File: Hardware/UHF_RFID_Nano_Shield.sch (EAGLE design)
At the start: 35 parts, among them J2 FTDI, J3 JST, J4 U.FL, J5 Extra, J6 Screw Terminal, J7 GPIOs, U1 Nano, U2 TXB0104, U3 TVS_DIODE_ARRAY

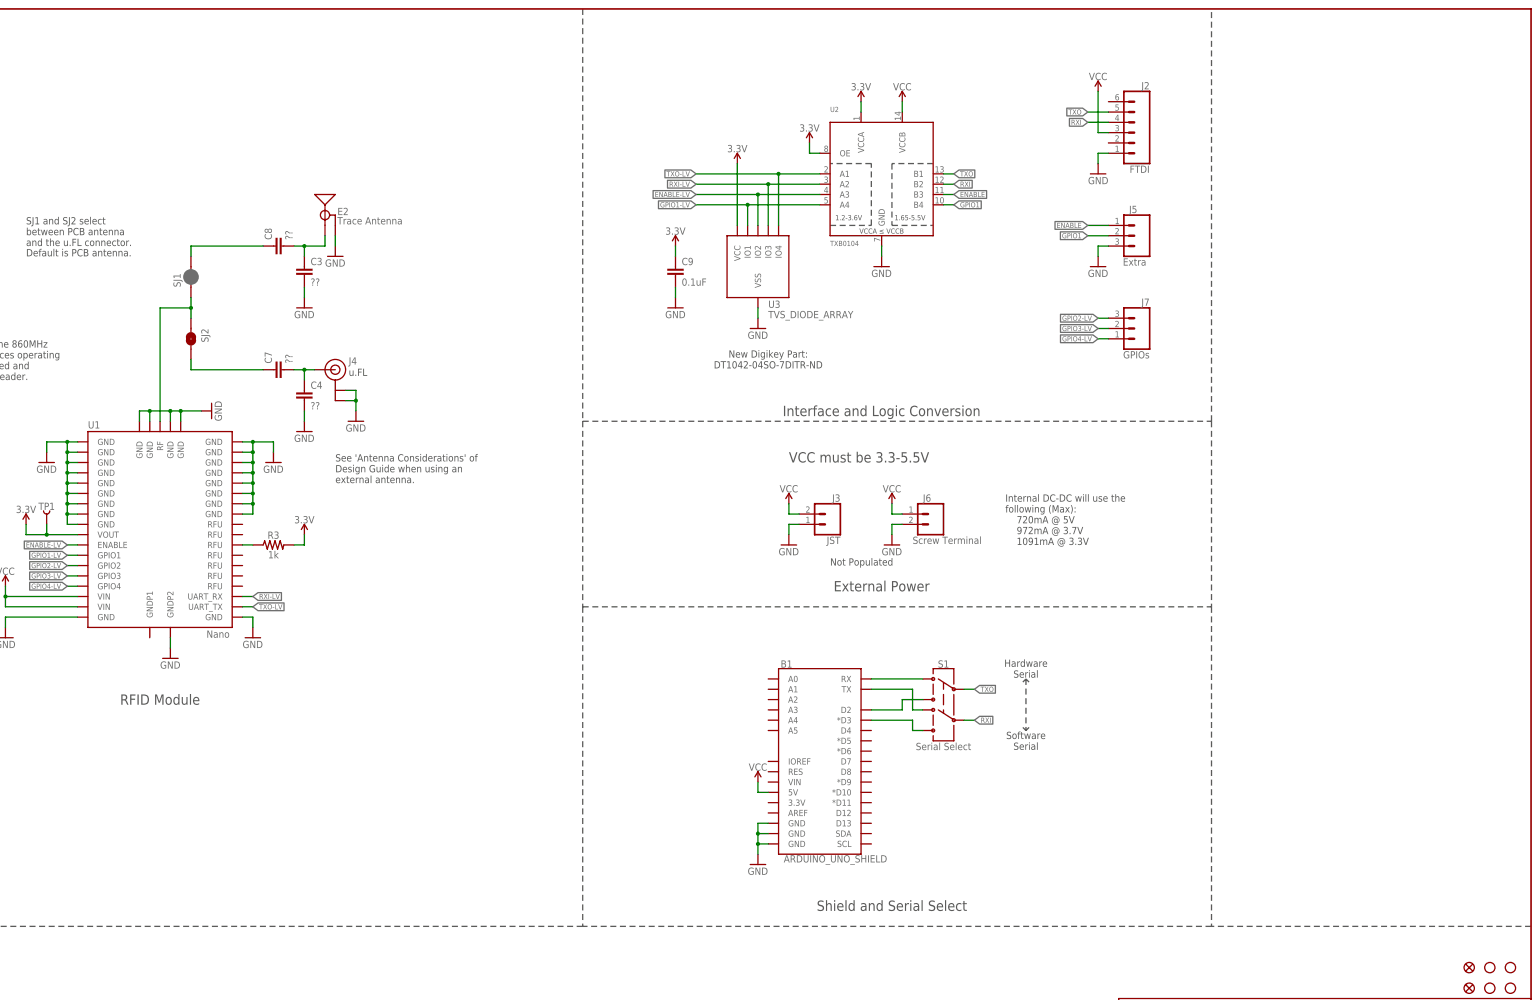
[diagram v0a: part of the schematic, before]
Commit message: Many changes from design review
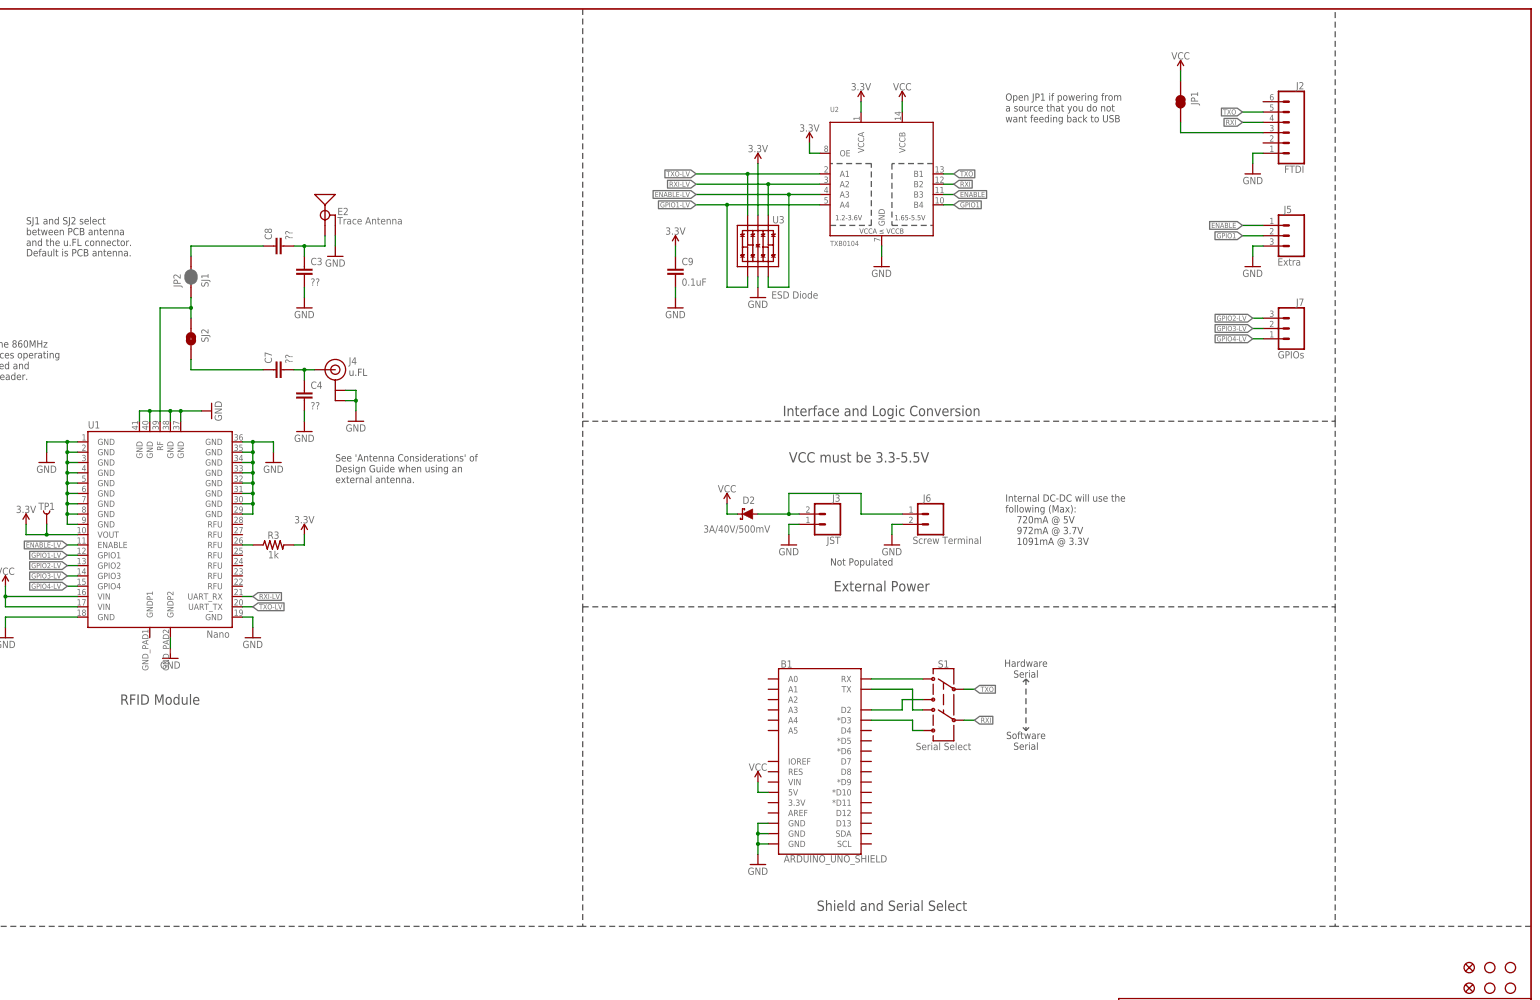
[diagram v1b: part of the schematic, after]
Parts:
- removed SJ1: JUMPER-SMT_2_NC_PASTE_NO-SILK, SparkFun-Jumpers:JUMPER-SMT_2_NC_PASTE_NO-SILK
- added D2: 3A/40V/500mV, SparkFun-DiscreteSemi:DIODE-SCHOTTKY-B340A
- added JP1: JUMPER-SMT_2_NC_TRACE_SILK, SparkFun-Jumpers:JUMPER-SMT_2_NC_TRACE_SILK
- added JP2: SJ1, SparkFun-Jumpers:JUMPER-SMT_2_NO_NO-SILK
- U3: value TVS_DIODE_ARRAY -> ESD Diode; device UHF_RFID_Nano_Module:TVS_DIODE_ARRAY -> UHF_RFID_Nano_Module:TVS_DIODE_ARRAYSMD
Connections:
- new net N$12: D2.A, J3.2, J6.1
- new net N$7: J2.3, JP1.2
- net ANT3: now also JP2.1; no longer SJ1.1
- net N$2: now also JP2.2; no longer SJ1.2
- net VCC: now also D2.C, JP1.1; no longer J2.3, J3.2, J6.1
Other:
- note added: "Open JP1 if powering from a source that you do not want feeding back to USB"
- note removed: "New Digikey Part: DT1042‑04SO-7DITR-ND"
- moved on the sheet: J2, J5, J7
